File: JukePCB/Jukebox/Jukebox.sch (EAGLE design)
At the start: 32 parts, among them J1 RJ45

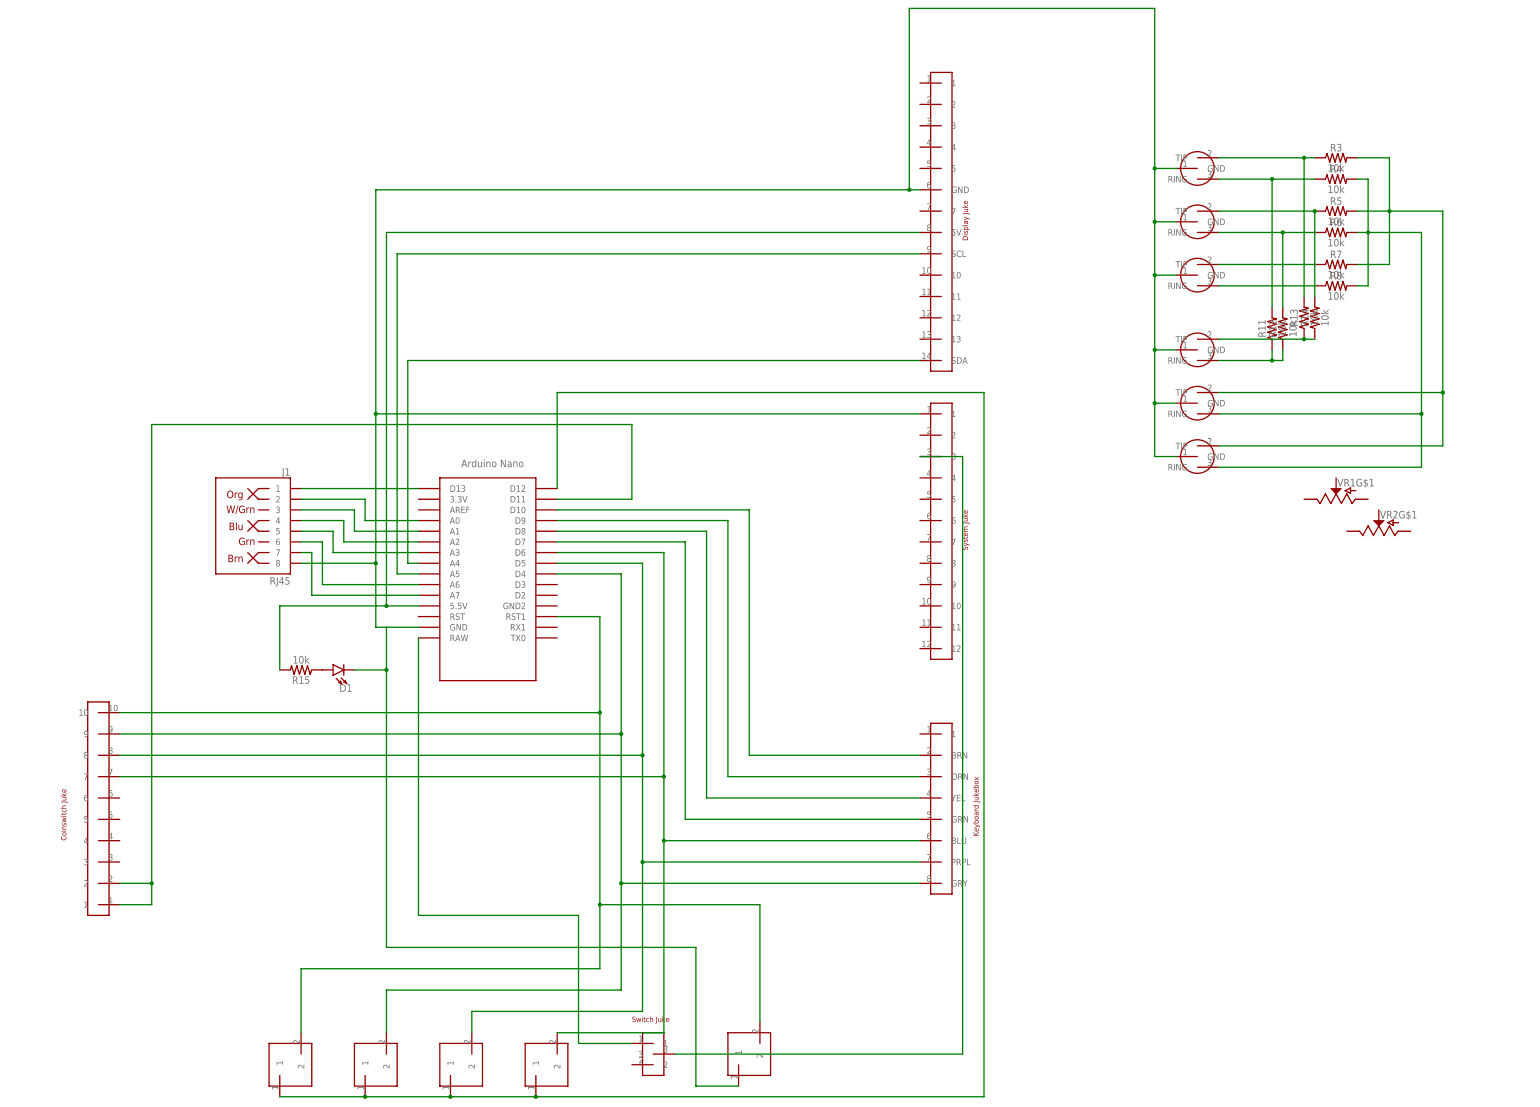
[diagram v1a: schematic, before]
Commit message: Added GND net
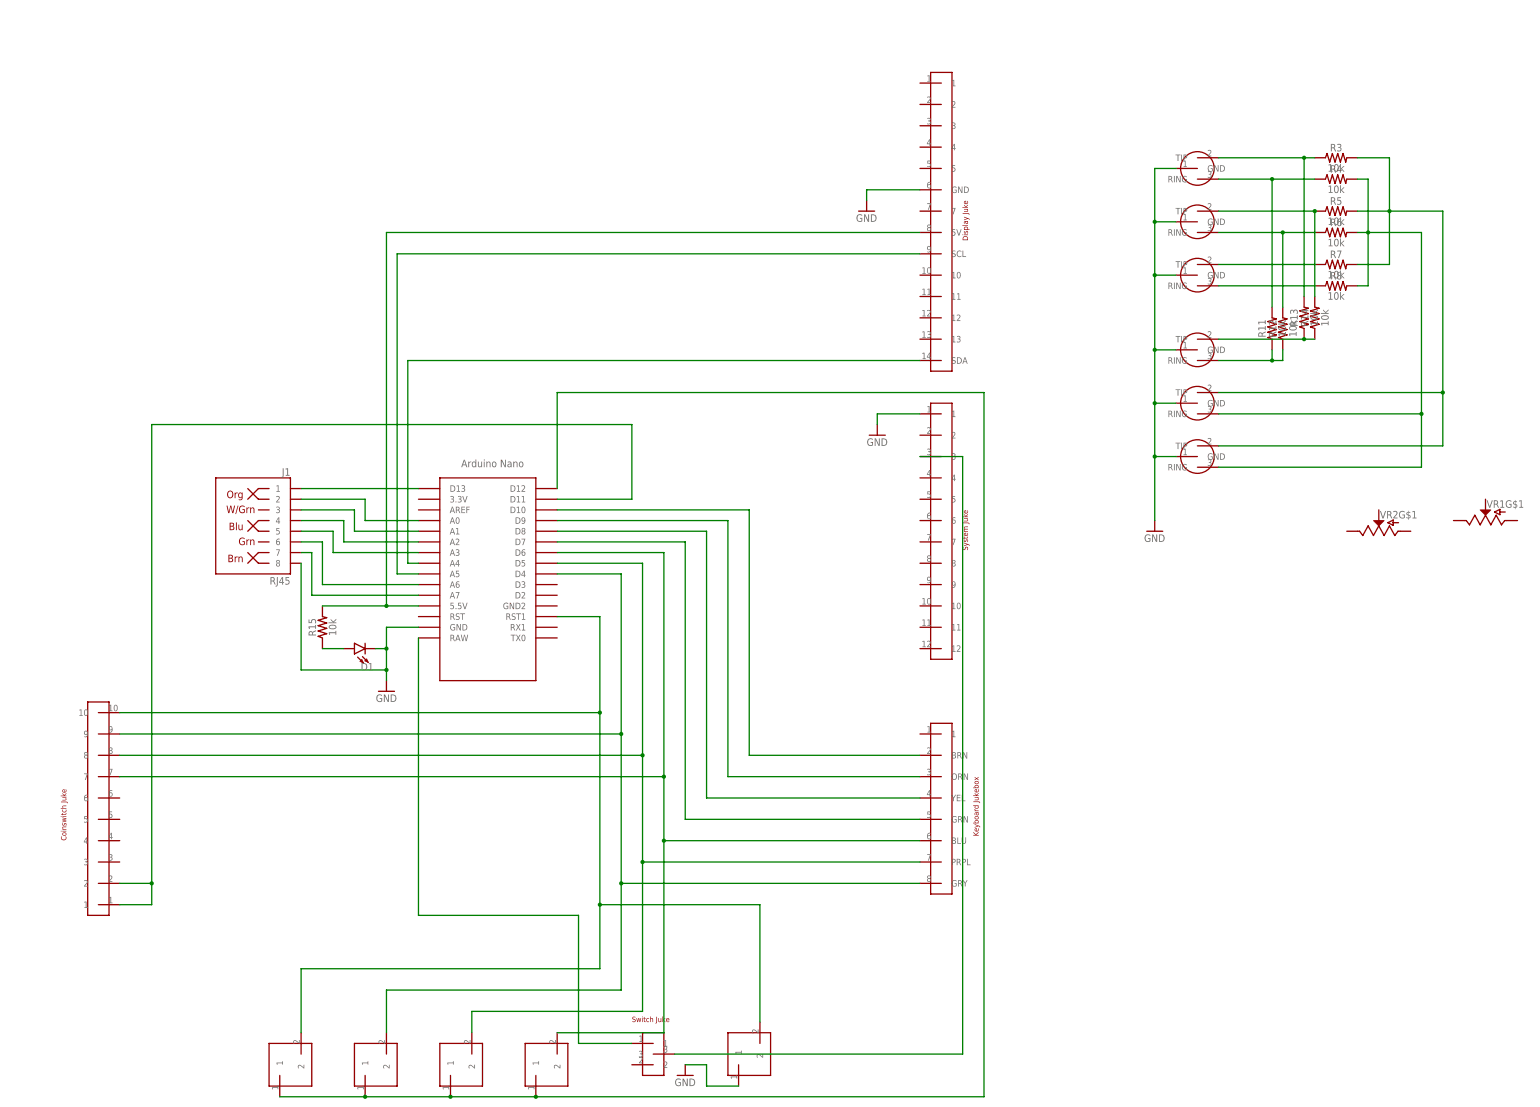
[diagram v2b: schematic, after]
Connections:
- net N$25 renamed GND
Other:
- moved on the sheet: D1, R15, VR1G$1
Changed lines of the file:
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@@
 <part name="D1" library="SparkFun-LED" deviceset="LED" device="5MM"/>
 <part name="VR2" library="SparkFun-Resistors" deviceset="POTENTIOMETER_DUAL" device="-PTH-12MM-1/20W-20%"/>
+<part name="GND1" library="supply1" deviceset="GND" device=""/>
+<part name="GND2" library="supply1" deviceset="GND" device=""/>
+<part name="GND3" library="supply1" deviceset="GND" device=""/>
+<part name="GND4" library="supply1" deviceset="GND" device=""/>
+<part name="GND5" library="supply1" deviceset="GND" device=""/>
 </parts>
 <sheets>
@@
 <instance part="R7" gate="G$1" x="226.06" y="60.96"/>
 <instance part="R8" gate="G$1" x="226.06" y="55.88"/>
-<instance part="VR1" gate="G$1" x="226.06" y="5.08" rot="R90"/>
+<instance part="VR1" gate="G$1" x="261.62" y="0" rot="R90"/>
 <instance part="U$2" gate="G$1" x="193.04" y="15.24" rot="R90"/>
 <instance part="R11" gate="G$1" x="210.82" y="45.72" rot="R90"/>
@@
 <instance part="R14" gate="G$1" x="220.98" y="48.26" rot="R90"/>
 <instance part="J1" gate="JP1" x="-27.94" y="0" rot="MR0"/>
-<instance part="R15" gate="G$1" x="-20.32" y="-35.56" rot="R180"/>
-<instance part="D1" gate="G$1" x="-12.7" y="-35.56" rot="R90"/>
+<instance part="R15" gate="G$1" x="-15.24" y="-25.4" rot="R90"/>
+<instance part="D1" gate="G$1" x="-7.62" y="-30.48" rot="R90"/>
 <instance part="VR2" gate="G$1" x="236.22" y="-2.54" rot="R90"/>
+<instance part="GND1" gate="1" x="182.88" y="-2.54"/>
+<instance part="GND2" gate="1" x="114.3" y="73.66"/>
+<instance part="GND3" gate="1" x="116.84" y="20.32"/>
+<instance part="GND4" gate="1" x="71.12" y="-132.08"/>
+<instance part="GND5" gate="1" x="0" y="-40.64"/>
 </instances>
 <busses>
@@
 </segment>
 </net>
-<net name="N$25" class="0">
-<segment>
-<pinref part="U$16" gate="G$1" pin="GND"/>
-<wire x1="187.96" y1="27.94" x2="182.88" y2="27.94" width="0.1524" layer="91"/>
-<wire x1="182.88" y1="27.94" x2="182.88" y2="40.64" width="0.1524" layer="91"/>
-<pinref part="U$15" gate="G$1" pin="GND"/>
-<wire x1="182.88" y1="40.64" x2="187.96" y2="40.64" width="0.1524" layer="91"/>
-<wire x1="182.88" y1="40.64" x2="182.88" y2="58.42" width="0.1524" layer="91"/>
-<junction x="182.88" y="40.64"/>
-<pinref part="U$4" gate="G$1" pin="GND"/>
-<wire x1="182.88" y1="58.42" x2="187.96" y2="58.42" width="0.1524" layer="91"/>
-<wire x1="182.88" y1="58.42" x2="182.88" y2="71.12" width="0.1524" layer="91"/>
-<junction x="182.88" y="58.42"/>
-<pinref part="U$3" gate="G$1" pin="GND"/>
-<wire x1="182.88" y1="71.12" x2="187.96" y2="71.12" width="0.1524" layer="91"/>
-<wire x1="182.88" y1="71.12" x2="182.88" y2="83.82" width="0.1524" layer="91"/>
-<junction x="182.88" y="71.12"/>
-<pinref part="AUXIN" gate="G$1" pin="GND"/>
-<wire x1="182.88" y1="83.82" x2="187.96" y2="83.82" width="0.1524" layer="91"/>
-<wire x1="182.88" y1="83.82" x2="182.88" y2="121.92" width="0.1524" layer="91"/>
-<junction x="182.88" y="83.82"/>
-<pinref part="U$7" gate="G$1" pin="GND"/>
-<wire x1="127" y1="78.74" x2="124.46" y2="78.74" width="0.1524" layer="91"/>
-<wire x1="124.46" y1="78.74" x2="-2.54" y2="78.74" width="0.1524" layer="91"/>
-<wire x1="-2.54" y1="78.74" x2="-2.54" y2="25.4" width="0.1524" layer="91"/>
-<wire x1="-2.54" y1="25.4" x2="-2.54" y2="-10.16" width="0.1524" layer="91"/>
-<pinref part="U$1" gate="G$1" pin="GND"/>
-<wire x1="-2.54" y1="-10.16" x2="-2.54" y2="-25.4" width="0.1524" layer="91"/>
-<wire x1="0" y1="-25.4" x2="7.62" y2="-25.4" width="0.1524" layer="91"/>
-<pinref part="U$8" gate="G$1" pin="1"/>
-<wire x1="127" y1="25.4" x2="-2.54" y2="25.4" width="0.1524" layer="91"/>
-<junction x="-2.54" y="25.4"/>
-<wire x1="182.88" y1="121.92" x2="124.46" y2="121.92" width="0.1524" layer="91"/>
-<wire x1="124.46" y1="121.92" x2="124.46" y2="78.74" width="0.1524" layer="91"/>
-<junction x="124.46" y="78.74"/>
-<pinref part="U$2" gate="G$1" pin="GND"/>
-<wire x1="187.96" y1="15.24" x2="182.88" y2="15.24" width="0.1524" layer="91"/>
-<wire x1="182.88" y1="15.24" x2="182.88" y2="27.94" width="0.1524" layer="91"/>
-<junction x="182.88" y="27.94"/>
-<pinref part="J1" gate="JP1" pin="8"/>
-<wire x1="-20.32" y1="-10.16" x2="-2.54" y2="-10.16" width="0.1524" layer="91"/>
-<junction x="-2.54" y="-10.16"/>
-<wire x1="-2.54" y1="-25.4" x2="0" y2="-25.4" width="0.1524" layer="91"/>
-<wire x1="0" y1="-25.4" x2="0" y2="-35.56" width="0.1524" layer="91"/>
-<pinref part="U$13" gate="G$1" pin="1"/>
-<wire x1="0" y1="-35.56" x2="0" y2="-101.6" width="0.1524" layer="91"/>
-<wire x1="83.82" y1="-134.62" x2="73.66" y2="-134.62" width="0.1524" layer="91"/>
-<wire x1="73.66" y1="-134.62" x2="73.66" y2="-101.6" width="0.1524" layer="91"/>
-<wire x1="0" y1="-101.6" x2="73.66" y2="-101.6" width="0.1524" layer="91"/>
-<pinref part="D1" gate="G$1" pin="C"/>
-<wire x1="-7.62" y1="-35.56" x2="0" y2="-35.56" width="0.1524" layer="91"/>
-<junction x="0" y="-35.56"/>
-</segment>
-</net>
 <net name="N$13" class="0">
 <segment>
@@
 <wire x1="0" y1="-20.32" x2="7.62" y2="-20.32" width="0.1524" layer="91"/>
 <pinref part="R15" gate="G$1" pin="2"/>
-<wire x1="-25.4" y1="-35.56" x2="-25.4" y2="-20.32" width="0.1524" layer="91"/>
-<wire x1="-25.4" y1="-20.32" x2="0" y2="-20.32" width="0.1524" layer="91"/>
+<wire x1="-15.24" y1="-20.32" x2="0" y2="-20.32" width="0.1524" layer="91"/>
 <junction x="0" y="-20.32"/>
 </segment>
@@
 <pinref part="R15" gate="G$1" pin="1"/>
 <pinref part="D1" gate="G$1" pin="A"/>
+<wire x1="-15.24" y1="-30.48" x2="-10.16" y2="-30.48" width="0.1524" layer="91"/>
 </segment>
 </net>
@@
 </segment>
 </net>
+<net name="GND" class="0">
+<segment>
+<pinref part="AUXIN" gate="G$1" pin="GND"/>
+<wire x1="182.88" y1="83.82" x2="187.96" y2="83.82" width="0.1524" layer="91"/>
+<pinref part="U$3" gate="G$1" pin="GND"/>
+<pinref part="U$4" gate="G$1" pin="GND"/>
+<pinref part="U$15" gate="G$1" pin="GND"/>
+<pinref part="U$16" gate="G$1" pin="GND"/>
+<wire x1="187.96" y1="27.94" x2="182.88" y2="27.94" width="0.1524" layer="91"/>
+<pinref part="GND1" gate="1" pin="GND"/>
+<pinref part="U$2" gate="G$1" pin="GND"/>
+<wire x1="187.96" y1="15.24" x2="182.88" y2="15.24" width="0.1524" layer="91"/>
+<wire x1="182.88" y1="15.24" x2="182.88" y2="0" width="0.1524" layer="91"/>
+<junction x="182.88" y="15.24"/>
+<wire x1="182.88" y1="15.24" x2="182.88" y2="27.94" width="0.1524" layer="91"/>
+<junction x="182.88" y="27.94"/>
+<wire x1="182.88" y1="27.94" x2="182.88" y2="40.64" width="0.1524" layer="91"/>
+<wire x1="182.88" y1="40.64" x2="187.96" y2="40.64" width="0.1524" layer="91"/>
+<junction x="182.88" y="40.64"/>
+<wire x1="182.88" y1="40.64" x2="182.88" y2="58.42" width="0.1524" layer="91"/>
+<wire x1="182.88" y1="58.42" x2="187.96" y2="58.42" width="0.1524" layer="91"/>
+<junction x="182.88" y="58.42"/>
+<wire x1="182.88" y1="58.42" x2="182.88" y2="71.12" width="0.1524" layer="91"/>
+<wire x1="182.88" y1="71.12" x2="187.96" y2="71.12" width="0.1524" layer="91"/>
+<wire x1="182.88" y1="71.12" x2="182.88" y2="83.82" width="0.1524" layer="91"/>
+<junction x="182.88" y="71.12"/>
+</segment>
+<segment>
+<pinref part="U$7" gate="G$1" pin="GND"/>
+<pinref part="GND2" gate="1" pin="GND"/>
+<wire x1="127" y1="78.74" x2="114.3" y2="78.74" width="0.1524" layer="91"/>
+<wire x1="114.3" y1="78.74" x2="114.3" y2="76.2" width="0.1524" layer="91"/>
+</segment>
+<segment>
+<pinref part="U$8" gate="G$1" pin="1"/>
+<pinref part="GND3" gate="1" pin="GND"/>
+<wire x1="127" y1="25.4" x2="116.84" y2="25.4" width="0.1524" layer="91"/>
+<wire x1="116.84" y1="25.4" x2="116.84" y2="22.86" width="0.1524" layer="91"/>
+</segment>
+<segment>
+<pinref part="U$13" gate="G$1" pin="1"/>
+<wire x1="83.82" y1="-134.62" x2="76.2" y2="-134.62" width="0.1524" layer="91"/>
+<wire x1="76.2" y1="-134.62" x2="76.2" y2="-129.54" width="0.1524" layer="91"/>
+<pinref part="GND4" gate="1" pin="GND"/>
+<wire x1="76.2" y1="-129.54" x2="71.12" y2="-129.54" width="0.1524" layer="91"/>
+</segment>
+<segment>
+<pinref part="GND5" gate="1" pin="GND"/>
+<pinref part="D1" gate="G$1" pin="C"/>
+<wire x1="-2.54" y1="-30.48" x2="0" y2="-30.48" width="0.1524" layer="91"/>
+<wire x1="0" y1="-30.48" x2="0" y2="-35.56" width="0.1524" layer="91"/>
+<junction x="0" y="-30.48"/>
+<wire x1="0" y1="-35.56" x2="0" y2="-38.1" width="0.1524" layer="91"/>
+<wire x1="0" y1="-25.4" x2="0" y2="-30.48" width="0.1524" layer="91"/>
+<pinref part="U$1" gate="G$1" pin="GND"/>
+<wire x1="7.62" y1="-25.4" x2="0" y2="-25.4" width="0.1524" layer="91"/>
+<pinref part="J1" gate="JP1" pin="8"/>
+<wire x1="-20.32" y1="-10.16" x2="-20.32" y2="-35.56" width="0.1524" layer="91"/>
+<wire x1="0" y1="-35.56" x2="-20.32" y2="-35.56" width="0.1524" layer="91"/>
+<junction x="0" y="-35.56"/>
+</segment>
+</net>

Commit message: smol update
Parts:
- removed VR1, VR2: (no value), SparkFun-Resistors:POTENTIOMETER_DUAL-PTH-12MM-1/20W-20%
- added JP1: (no value), adafruit:PINHD-1X6
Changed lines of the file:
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@@
 <layer number="230" name="230bmp" color="7" fill="1" visible="yes" active="yes"/>
 <layer number="231" name="231bmp" color="7" fill="1" visible="yes" active="yes"/>
+<layer number="232" name="Eagle3D_PG2" color="7" fill="1" visible="no" active="no"/>
+<layer number="233" name="Eagle3D_PG3" color="7" fill="1" visible="no" active="no"/>
 <layer number="248" name="Housing" color="7" fill="1" visible="yes" active="yes"/>
 <layer number="249" name="Edge" color="7" fill="1" visible="yes" active="yes"/>
@@
 <part name="R7" library="SparkFun-Resistors" deviceset="10KOHM" device="-HORIZ-1/4W-1%" value="10k"/>
 <part name="R8" library="SparkFun-Resistors" deviceset="10KOHM" device="-HORIZ-1/4W-1%" value="10k"/>
-<part name="VR1" library="SparkFun-Resistors" deviceset="POTENTIOMETER_DUAL" device="-PTH-12MM-1/20W-20%"/>
 <part name="U$2" library="Jukebox" deviceset="JUKEHEADPHONE" device=""/>
 <part name="R11" library="SparkFun-Resistors" deviceset="10KOHM" device="-HORIZ-1/4W-1%" value="10k"/>
@@
 <part name="R15" library="SparkFun-Resistors" deviceset="10KOHM" device="-HORIZ-1/4W-1%" value="10k"/>
 <part name="D1" library="SparkFun-LED" deviceset="LED" device="5MM"/>
-<part name="VR2" library="SparkFun-Resistors" deviceset="POTENTIOMETER_DUAL" device="-PTH-12MM-1/20W-20%"/>
 <part name="GND1" library="supply1" deviceset="GND" device=""/>
 <part name="GND2" library="supply1" deviceset="GND" device=""/>
@@
 <part name="GND4" library="supply1" deviceset="GND" device=""/>
 <part name="GND5" library="supply1" deviceset="GND" device=""/>
+<part name="JP1" library="adafruit" deviceset="PINHD-1X6" device=""/>
 </parts>
 <sheets>
@@
 <instance part="R7" gate="G$1" x="226.06" y="60.96"/>
 <instance part="R8" gate="G$1" x="226.06" y="55.88"/>
-<instance part="VR1" gate="G$1" x="261.62" y="0" rot="R90"/>
 <instance part="U$2" gate="G$1" x="193.04" y="15.24" rot="R90"/>
 <instance part="R11" gate="G$1" x="210.82" y="45.72" rot="R90"/>
@@
 <instance part="R15" gate="G$1" x="-15.24" y="-25.4" rot="R90"/>
 <instance part="D1" gate="G$1" x="-7.62" y="-30.48" rot="R90"/>
-<instance part="VR2" gate="G$1" x="236.22" y="-2.54" rot="R90"/>
 <instance part="GND1" gate="1" x="182.88" y="-2.54"/>
 <instance part="GND2" gate="1" x="114.3" y="73.66"/>
@@
 <instance part="GND4" gate="1" x="71.12" y="-132.08"/>
 <instance part="GND5" gate="1" x="0" y="-40.64"/>
+<instance part="JP1" gate="A" x="203.2" y="109.22" rot="R90"/>
 </instances>
 <busses>

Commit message: almost final schematic
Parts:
- removed AUXIN: JUKEHEADPHONE, Jukebox:JUKEHEADPHONE
- removed JP1: (no value), adafruit:PINHD-1X6
- removed R11, R12, R13, R14, R3, R4: 10k, SparkFun-Resistors:10KOHM-HORIZ-1/4W-1%
- added CN1: 1X4-BIG, adafruit:1X4-BIG
- added J2: (no value), SparkFun-Connectors:CONN_02
- added J3, J4, J5, J6: (no value), SparkFun-Connectors:CONN_01
- added U$17: 8PINJUKE2, Jukebox:8PINJUKE2
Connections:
- new net N$22: U$1.D3, U$17.ADDCOINS
- new net N$25: U$1.D2, U$17.NOWPLAYING
- new net N$34: U$1.RX1, U$17.YOURSELECTION
- new net N$37: U$1.TX0, U$17.RST
- net GND: now also J3.1; no longer AUXIN.GND
- net N$13: now also CN1.3; no longer R13.1, R14.1
- net N$14: now also CN1.4, U$15.RING; no longer AUXIN.TIP, R13.2, R3.1
- net N$15: now also J2.2, J5.1; no longer AUXIN.RING, R11.2, R4.1
- net N$16: no longer R12.2
- net N$17: no longer R14.2
- net N$18: now also CN1.2
- net N$19: now also CN1.1
- net N$20: now also J2.1, J6.1; no longer R11.1, R12.1, U$15.RING
- net N$23: no longer R4.2
- net N$24: no longer R3.2
- net N$27: now also U$17.VCC
- net N$8: now also J4.1
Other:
- note added: "Amp In"
- note added: "Aux In"
- note added: "Aux out"
- note added: "Light In"
- note added: "Needle"

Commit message: Huge board update
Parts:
- removed J1: RJ45, SparkFun-Connectors:RJ45-8
- added CONTROL1, CONTROL2: 1X4-BIG, adafruit:1X4-BIG
- renumbered R5 to N1, R6 to N2, R7 to A1, R8 to A2, U$15 to TOAMP, U$16 to AUXOUT, U$2 to TOLIGHT, U$3 to FROMNEEDLE, U$4 to AUXIN
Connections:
- net GND: now also CONTROL2.1; no longer J1.8
- net N$1: now also U$5.7, U$9.2; no longer U$10.2, U$5.9
- net N$2: now also U$10.2; no longer U$11.2
- net N$26: now also CONTROL1.4; no longer J1.1
- net N$28: now also CONTROL1.3; no longer J1.2
- net N$29: now also CONTROL1.2; no longer J1.3
- net N$3: now also U$11.2, U$5.9; no longer U$12.2, U$5.7
- net N$30: now also CONTROL1.1; no longer J1.4
- net N$31: now also CONTROL2.4; no longer J1.5
- net N$35: now also CONTROL2.3; no longer J1.6
- net N$36: now also CONTROL2.2; no longer J1.7
- net N$4: now also U$12.2, U$5.10
- net N$9: no longer U$5.10, U$9.2
